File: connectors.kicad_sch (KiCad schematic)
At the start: 18 parts, among them J2 Conn_WS2812_Extern, T7 AO3400A, T8 AO3400A, X10 S4B-PH-SM4-K-TB(LF)(SN), X13 KF2EDGR-3.81-3P, X5 KF2EDGR-3.81-3P, X7 BH-00105, X8 USB3.1C16PFSMT

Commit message: layout done so far. Have to check everything again
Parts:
- J2, X6: now left out of the parts list
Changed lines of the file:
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@@
   )
   (symbol (lib_id "Connector_Generic:Conn_01x03") (at 253.365 88.265 0) (unit 1)
-    (in_bom yes) (on_board yes) (dnp no)
+    (in_bom no) (on_board yes) (dnp no)
     (property "Reference" "J2" (at 255.397 87.4303 0)
       (effects (font (size 1.27 1.27)) (justify left))
@@
   )
   (symbol (lib_id "EduboardV2_kicadlib:protoboard_patch") (at 185.42 102.87 0) (unit 1)
-    (in_bom yes) (on_board yes) (dnp no) (fields_autoplaced)
+    (in_bom no) (on_board yes) (dnp no) (fields_autoplaced)
     (property "Reference" "X6" (at 205.74 124.968 0)
       (effects (font (size 1.27 1.27)) (justify left))

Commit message: finalize baseboard. finishing touches
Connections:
- net GND: no longer X7.39
- net V_EXT: now also X7.39
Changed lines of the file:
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@@
   (junction (at 61.595 98.425) (diameter 0) (color 0 0 0 0)
-  )
-  (junction (at 41.275 98.425) (diameter 0) (color 0 0 0 0)
   )
   (junction (at 241.935 153.035) (diameter 0) (color 0 0 0 0)
@@
     (stroke (width 0) (type default))
   )
-  (wire (pts (xy 41.275 52.705) (xy 44.45 52.705))
-    (stroke (width 0) (type default))
-  )
   (wire (pts (xy 59.69 98.425) (xy 61.595 98.425))
     (stroke (width 0) (type default))
@@
     (stroke (width 0) (type default))
   )
+  (wire (pts (xy 41.91 101.6) (xy 41.91 98.425))
+    (stroke (width 0) (type default))
+  )
   (wire (pts (xy 247.65 71.755) (xy 243.84 71.755))
     (stroke (width 0) (type default))
   )
+  (wire (pts (xy 41.91 98.425) (xy 44.45 98.425))
+    (stroke (width 0) (type default))
+  )
   (wire (pts (xy 175.895 97.79) (xy 179.07 97.79))
     (stroke (width 0) (type default))
@@
     (stroke (width 0) (type default))
   )
+  (wire (pts (xy 34.29 46.355) (xy 34.29 52.705))
+    (stroke (width 0) (type default))
+  )
   (wire (pts (xy 175.895 124.46) (xy 179.07 124.46))
     (stroke (width 0) (type default))
@@
     (stroke (width 0) (type default))
   )
-  (wire (pts (xy 41.275 98.425) (xy 44.45 98.425))
-    (stroke (width 0) (type default))
-  )
   (wire (pts (xy 59.69 88.265) (xy 63.5 88.265))
     (stroke (width 0) (type default))
@@
     (stroke (width 0) (type default))
   )
+  (wire (pts (xy 34.29 52.705) (xy 44.45 52.705))
+    (stroke (width 0) (type default))
+  )
   (wire (pts (xy 175.895 109.22) (xy 179.07 109.22))
     (stroke (width 0) (type default))
@@
     (stroke (width 0) (type default))
   )
-  (wire (pts (xy 41.275 98.425) (xy 41.275 52.705))
-    (stroke (width 0) (type default))
-  )
   (wire (pts (xy 38.1 80.645) (xy 44.45 80.645))
     (stroke (width 0) (type default))
@@
   )
   (wire (pts (xy 59.69 70.485) (xy 63.5 70.485))
-    (stroke (width 0) (type default))
-  )
-  (wire (pts (xy 41.275 101.6) (xy 41.275 98.425))
     (stroke (width 0) (type default))
   )
@@
         (path "/280adf03-05ea-4001-ab24-a5a43e6d4cc9/bbe51f60-6efe-4402-8542-2dfbd71b2c52"
           (reference "#PWR0115") (unit 1)
+        )
+      )
+    )
+  )
+  (symbol (lib_id "eduboardv2:GND") (at 34.29 46.355 180) (unit 1)
+    (in_bom yes) (on_board yes) (dnp no) (fields_autoplaced)
+    (property "Reference" "#PWR097" (at 34.29 40.005 0)
+      (effects (font (size 1.27 1.27)) hide)
+    )
+    (property "Value" "GND" (at 34.29 42.545 0)
+      (effects (font (size 1.27 1.27)))
+    )
+    (property "Footprint" "" (at 34.29 46.355 0)
+      (effects (font (size 1.27 1.27)) hide)
+    )
+    (property "Datasheet" "" (at 34.29 46.355 0)
+      (effects (font (size 1.27 1.27)) hide)
+    )
+    (pin "1")
+    (instances
+      (project "EduboardV2_Baseboard"
+        (path "/280adf03-05ea-4001-ab24-a5a43e6d4cc9/dc18459b-bf67-402d-bc74-ca4debdbcff4"
+          (reference "#PWR097") (unit 1)
+        )
+        (path "/280adf03-05ea-4001-ab24-a5a43e6d4cc9/bbe51f60-6efe-4402-8542-2dfbd71b2c52"
+          (reference "#PWR0153") (unit 1)
         )
       )
@@
     )
   )
+  (symbol (lib_name "V_EXT_1") (lib_id "eduboardv2:V_EXT") (at 41.91 101.6 180) (unit 1)
+    (in_bom yes) (on_board yes) (dnp no) (fields_autoplaced)
+    (property "Reference" "#PWR017" (at 41.91 97.79 0)
+      (effects (font (size 1.27 1.27)) hide)
+    )
+    (property "Value" "V_EXT" (at 41.91 106.68 0)
+      (effects (font (size 1.27 1.27)))
+    )
+    (property "Footprint" "" (at 41.91 101.6 0)
+      (effects (font (size 1.27 1.27)) hide)
+    )
+    (property "Datasheet" "" (at 41.91 101.6 0)
+      (effects (font (size 1.27 1.27)) hide)
+    )
+    (pin "1")
+    (instances
+      (project "EduboardV2_Baseboard"
+        (path "/280adf03-05ea-4001-ab24-a5a43e6d4cc9/5431a3ef-e3a9-462a-b9dc-2ffdf9ab7e55"
+          (reference "#PWR017") (unit 1)
+        )
+        (path "/280adf03-05ea-4001-ab24-a5a43e6d4cc9/bbe51f60-6efe-4402-8542-2dfbd71b2c52"
+          (reference "#PWR0200") (unit 1)
+        )
+      )
+    )
+  )
   (symbol (lib_id "eduboardv2:BH-00105") (at 52.07 70.485 0) (unit 1)
     (in_bom yes) (on_board yes) (dnp no)
@@
         )
       )
-    )
-  )
-  (symbol (lib_id "eduboardv2:GND") (at 41.275 101.6 0) (unit 1)
-    (in_bom yes) (on_board yes) (dnp no) (fields_autoplaced)
-    (property "Reference" "#PWR097" (at 41.275 107.95 0)
-      (effects (font (size 1.27 1.27)) hide)
-    )
-    (property "Value" "GND" (at 41.275 106.68 0)
-      (effects (font (size 1.27 1.27)))
-    )
-    (property "Footprint" "" (at 41.275 101.6 0)
-      (effects (font (size 1.27 1.27)) hide)
-    )
-    (property "Datasheet" "" (at 41.275 101.6 0)
-      (effects (font (size 1.27 1.27)) hide)
-    )
-    (pin "1")
-    (instances
-      (project "EduboardV2_Baseboard"
-        (path "/280adf03-05ea-4001-ab24-a5a43e6d4cc9/dc18459b-bf67-402d-bc74-ca4debdbcff4"
-          (reference "#PWR097") (unit 1)
-        )
-        (path "/280adf03-05ea-4001-ab24-a5a43e6d4cc9/bbe51f60-6efe-4402-8542-2dfbd71b2c52"
-          (reference "#PWR0153") (unit 1)
-        )
-      )

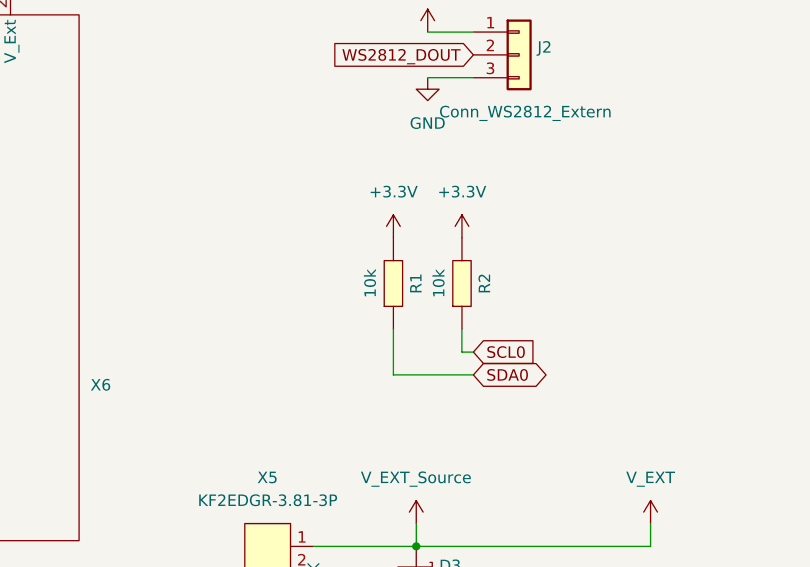
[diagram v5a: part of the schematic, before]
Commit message: fix some wrong jlcpcb part numbers
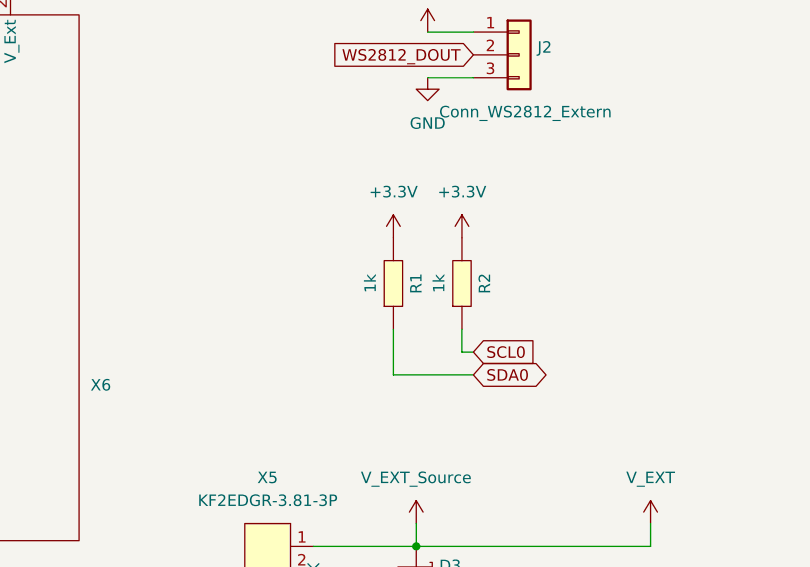
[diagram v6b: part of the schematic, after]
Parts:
- R1, R2: value 10k -> 1k; LCSC Part C25077 -> C11702
- R51, R52: LCSC Part C25077 -> C25744
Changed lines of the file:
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@@
       (effects (font (size 1.27 1.27)) hide)
     )
-    (property "LCSC Part" "C25077" (at 200.66 26.67 0)
+    (property "LCSC Part" "C25744" (at 200.66 26.67 0)
       (effects (font (size 1.27 1.27)) hide)
     )
@@
       (effects (font (size 1.27 1.27)))
     )
-    (property "Value" "10k" (at 244.475 113.665 0)
+    (property "Value" "1k" (at 244.475 113.665 0)
       (effects (font (size 1.27 1.27)))
     )
@@
       (effects (font (size 1.27 1.27)) hide)
     )
-    (property "LCSC Part" "C25077" (at 264.795 113.665 0)
+    (property "LCSC Part" "C11702" (at 264.795 113.665 0)
       (effects (font (size 1.27 1.27)) hide)
     )
@@
       (effects (font (size 1.27 1.27)) hide)
     )
-    (property "LCSC Part" "C25077" (at 200.66 6.35 0)
+    (property "LCSC Part" "C25744" (at 200.66 6.35 0)
       (effects (font (size 1.27 1.27)) hide)
     )
@@
       (effects (font (size 1.27 1.27)))
     )
-    (property "Value" "10k" (at 236.855 113.665 0)
+    (property "Value" "1k" (at 236.855 113.665 0)
       (effects (font (size 1.27 1.27)))
     )
@@
       (effects (font (size 1.27 1.27)) hide)
     )
-    (property "LCSC Part" "C25077" (at 257.175 113.665 0)
-      (effects (font (size 1.27 1.27)) hide)
-    )
+    (property "LCSC Part" "C11702" (at 257.175 113.665 0)
+      (effects (font (size 1.27 1.27)) hide)
+    )

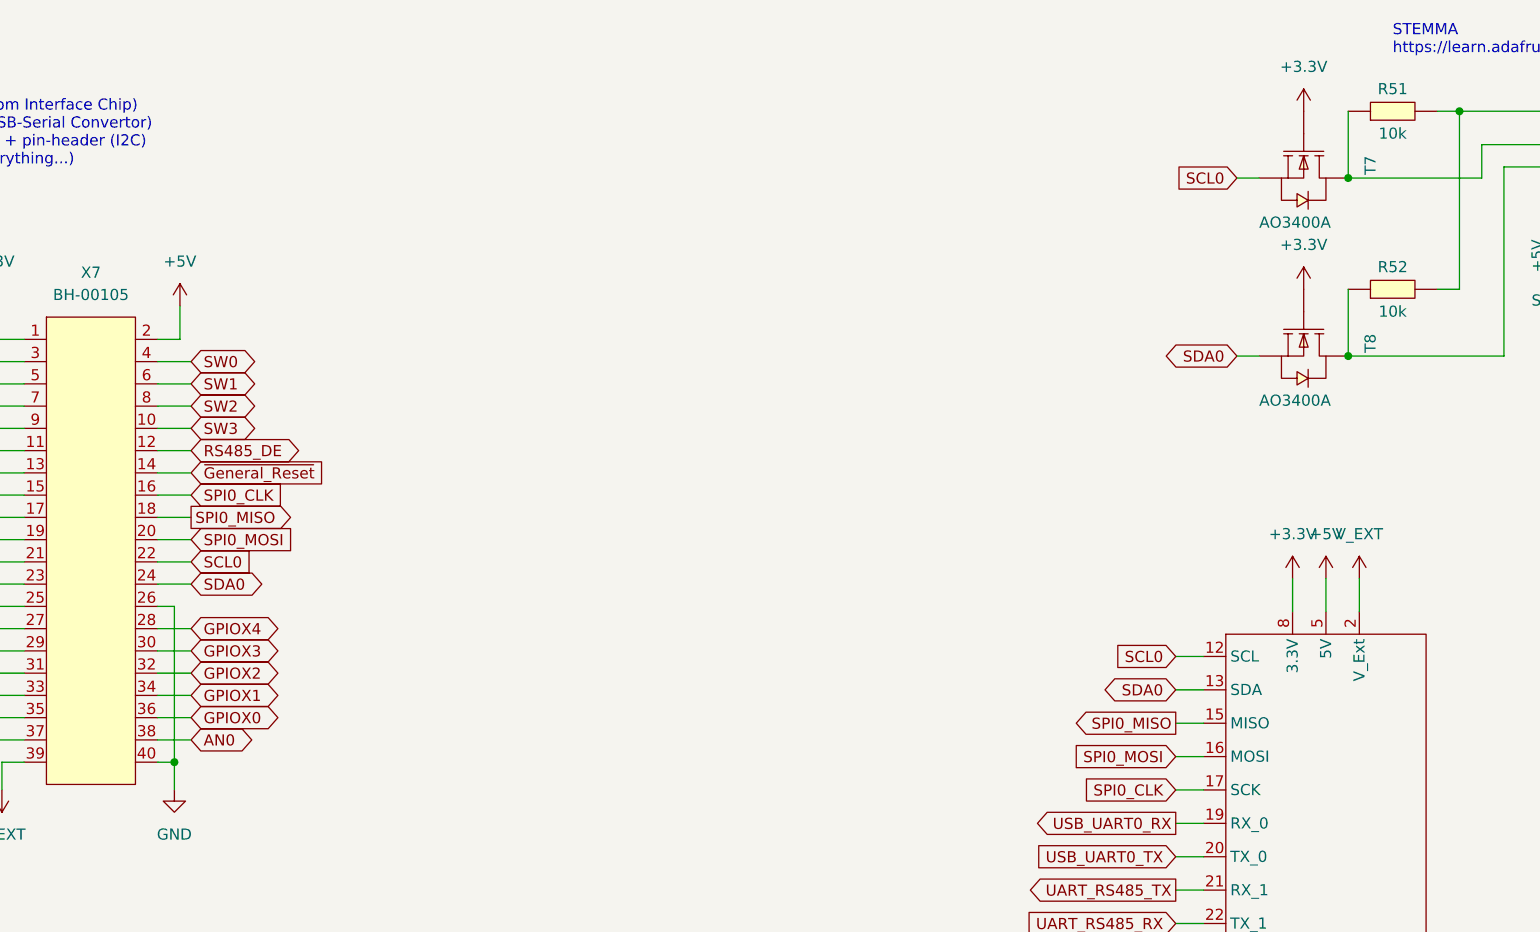
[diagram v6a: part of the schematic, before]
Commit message: add 2x DAC and fix I2C Impedance and Level Shifter
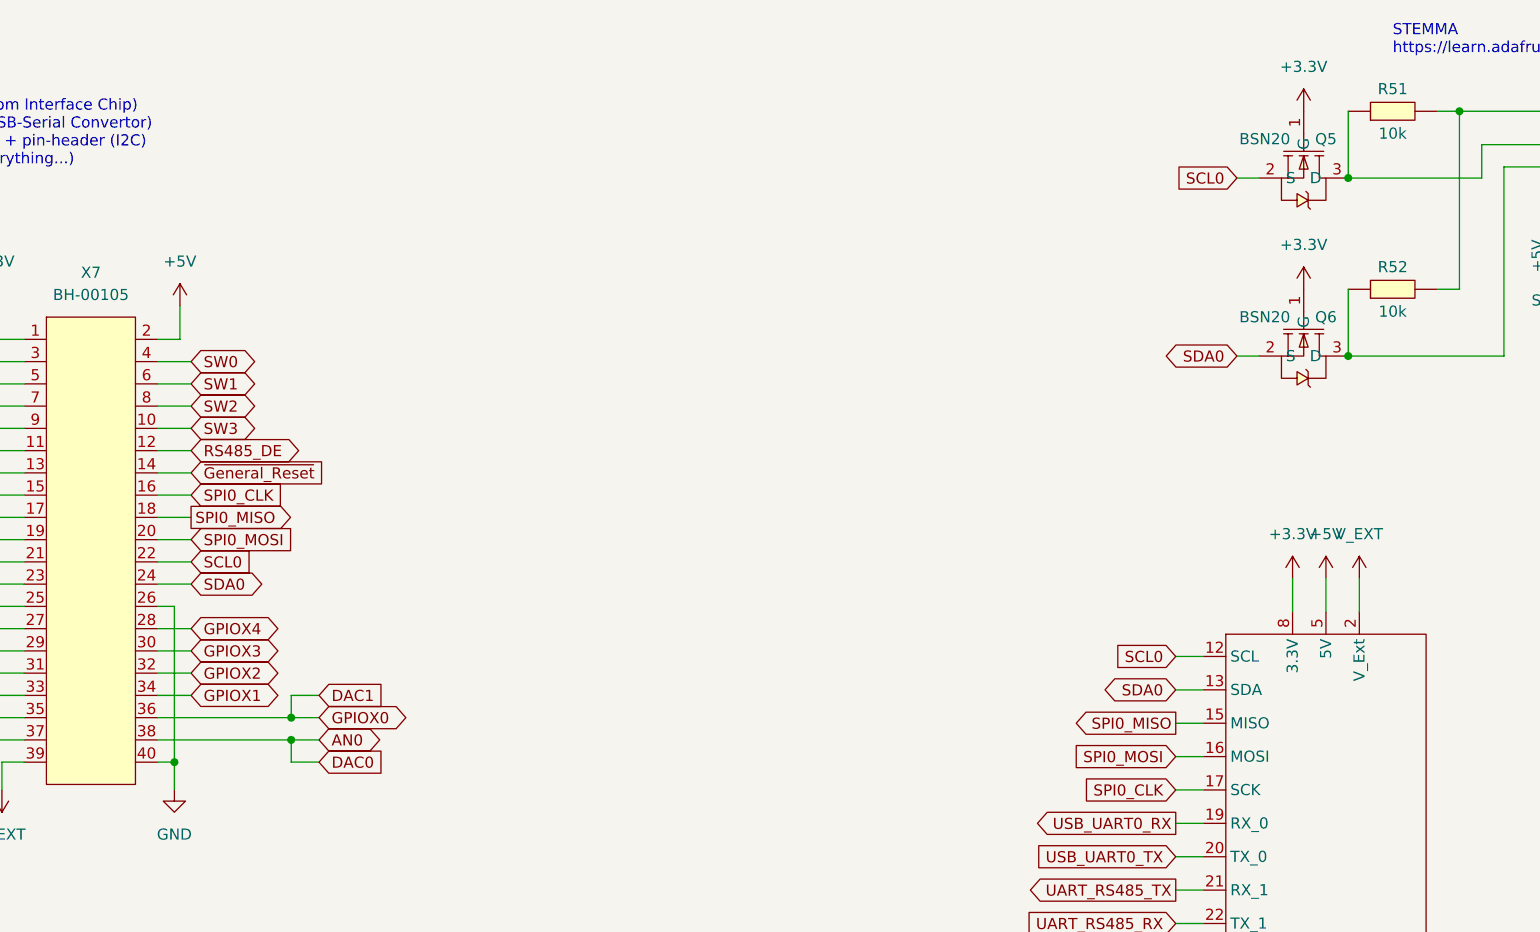
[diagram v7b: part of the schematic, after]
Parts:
- removed T7, T8: AO3400A, EduboardV2_kicadlib:SOT-23-3_L2.9-W1.6-P1.90-LS2.8-BR, symbol eduboardv2:AO3400A
- added Q5, Q6: BSN20, EduboardV2_kicadlib:SOT-23-3_L2.9-W1.6-P1.90-LS2.8-BR, symbol EduboardV2_kicadlib:BSN20
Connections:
- net +3.3V: now also Q5.1 (G), Q6.1 (G)
- net SCL0: now also Q5.2 (S)
- net SDA0: now also Q6.2 (S)
- net at R52.1, X10.2: now also Q6.3 (D)
- net at R51.1, X10.1: now also Q5.3 (D)
- net GPIOX0 renamed DAC1
